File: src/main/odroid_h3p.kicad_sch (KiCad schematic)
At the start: 2 parts, among them J301 Conn_02x12_Top_Bottom, J302 Conn_01x12

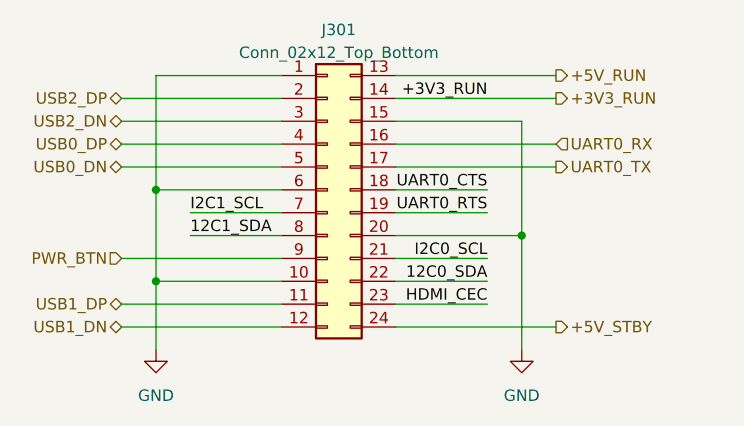
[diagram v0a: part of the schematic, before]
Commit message: Fix wrong header pinout
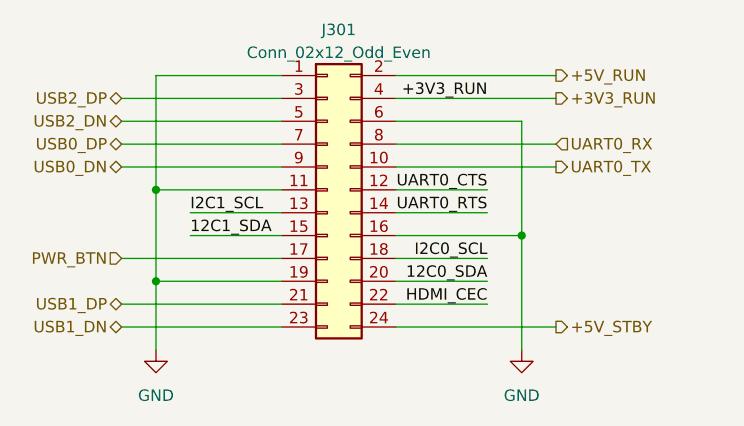
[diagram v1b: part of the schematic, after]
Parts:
- removed J301: Conn_02x12_Top_Bottom, odroid_h3_uitx_adapter:PinHeader_2x12_P2.54mm_Vertical, symbol odroid_h3_uitx_adapter:Conn_02x12_Top_Bottom
- added J301: Conn_02x12_Odd_Even, odroid_h3_uitx_adapter:PinHeader_2x12_P2.54mm_Vertical, symbol odroid_h3_uitx_adapter:Conn_02x12_Odd_Even
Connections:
- net +3V3_RUN: now also J301.4 (Pin_4)
- net +5V_RUN: now also J301.2 (Pin_2)
- net +5V_STBY: now also J301.24 (Pin_24)
- net 12C0_SDA: now also J301.20 (Pin_20)
- net 12C1_SDA: now also J301.15 (Pin_15)
- net GND: now also J301.1 (Pin_1), J301.11 (Pin_11), J301.16 (Pin_16), J301.19 (Pin_19), J301.6 (Pin_6)
- net HDMI_CEC: now also J301.22 (Pin_22)
- net I2C0_SCL: now also J301.18 (Pin_18)
- net I2C1_SCL: now also J301.13 (Pin_13)
- net PWR_BTN: now also J301.17 (Pin_17)
- net UART0_CTS: now also J301.12 (Pin_12)
- net UART0_RTS: now also J301.14 (Pin_14)
- net UART0_RX: now also J301.8 (Pin_8)
- net UART0_TX: now also J301.10 (Pin_10)
- net USB0_DN: now also J301.9 (Pin_9)
- net USB0_DP: now also J301.7 (Pin_7)
- net USB1_DN: now also J301.23 (Pin_23)
- net USB1_DP: now also J301.21 (Pin_21)
- net USB2_DN: now also J301.5 (Pin_5)
- net USB2_DP: now also J301.3 (Pin_3)
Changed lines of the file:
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@@
     )
   )
-  (symbol (lib_id "odroid_h3_uitx_adapter:Conn_02x12_Top_Bottom") (at 129.54 87.63 0) (unit 1)
+  (symbol (lib_id "odroid_h3_uitx_adapter:Conn_02x12_Odd_Even") (at 129.54 87.63 0) (unit 1)
     (in_bom yes) (on_board yes) (dnp no) (fields_autoplaced)
     (property "Reference" "J301" (at 129.54 69.85 0)
       (effects (font (size 1.27 1.27)))
     )
-    (property "Value" "Conn_02x12_Top_Bottom" (at 129.54 72.39 0)
+    (property "Value" "Conn_02x12_Odd_Even" (at 129.54 72.39 0)
       (effects (font (size 1.27 1.27)))
     )
-    (property "Footprint" "odroid_h3_uitx_adapter:PinHeader_2x12_P2.54mm_Vertical" (at 127 107.95 0)
+    (property "Footprint" "odroid_h3_uitx_adapter:PinHeader_2x12_P2.54mm_Vertical" (at 129.54 107.95 0)
       (effects (font (size 1.27 1.27)) hide)
     )
-    (property "Datasheet" "~" (at 128.27 87.63 0)
+    (property "Datasheet" "~" (at 129.54 113.03 0)
       (effects (font (size 1.27 1.27)) hide)
     )
-    (property "LCSC" "C2935922" (at 128.27 110.49 0)
+    (property "LCSC" "C2935922" (at 129.54 110.49 0)
       (effects (font (size 1.27 1.27)) hide)
     )

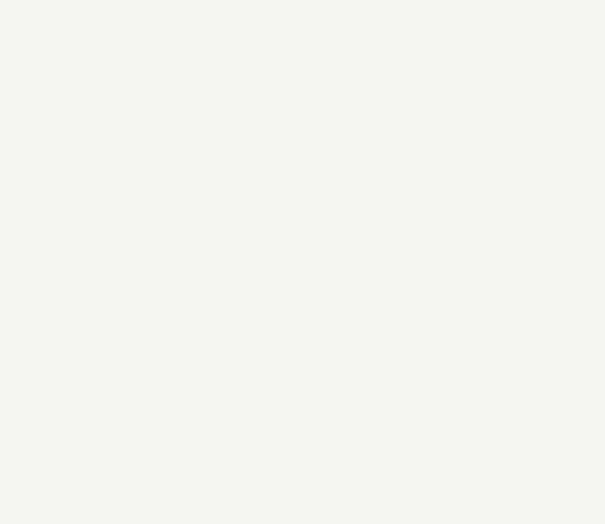
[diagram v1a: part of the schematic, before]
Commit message: rev1.1.0
- J201 programming header
  - Add reset button
  - Add enable button
  - Make pinout compatible with USB-UART boards
    - Move GPI0 and ENABLE to testpoints
- Add power rail LED status indicators
  - 3V3_RUN
  - 3V3_ESP32
  - 5V_RUN
  - 5V_STBY
  - VBUS_[1-3]
- Remove JP201
- Add GPIO39 external pullup to 3V3
- Add pulldown to PWR_BUTTON (GPIO15)
- Add github link
- Add sillkscreen alignment fixes
- Add silkscreen default jumper marking
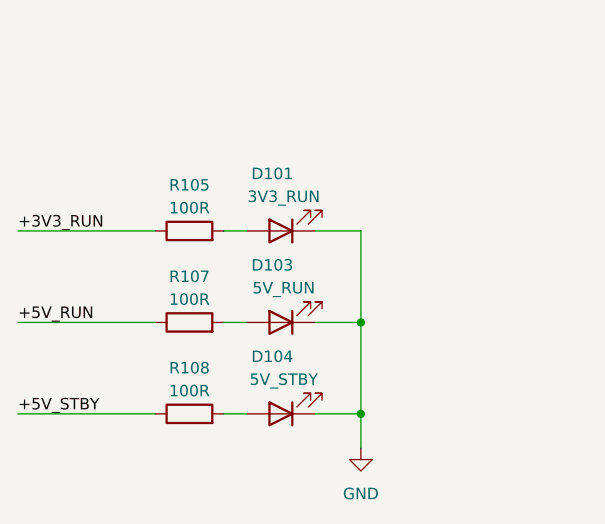
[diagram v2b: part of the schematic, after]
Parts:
- added D101: 3V3_RUN, LED_SMD:LED_0603_1608Metric, symbol Device:LED
- added D103: 5V_RUN, LED_SMD:LED_0603_1608Metric, symbol Device:LED
- added D104: 5V_STBY, LED_SMD:LED_0603_1608Metric, symbol Device:LED
- added R105, R107, R108: 100R, Resistor_SMD:R_0402_1005Metric, symbol Device:R
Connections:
- net +3V3_RUN: now also R105.1
- net +5V_RUN: now also R107.1
- net +5V_STBY: now also R108.1
- net GND: now also D101.1 (K), D103.1 (K), D104.1 (K)
- new net: D101.2 (A), R105.2
- new net: D103.2 (A), R107.2
- new net: D104.2 (A), R108.2
